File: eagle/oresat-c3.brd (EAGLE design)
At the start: 99.8 x 94.6 mm, 411 parts, among them IC2 STM32F439VIT6_PORT_BREAKOUT, J5 ORESAT-DEBUG-CONNECTOR-ALL, J6 J-SAMTEC-TFM-120-X1-XXX-D-RA, Q1 MOSFET-PCH-SOT23-6, Q10 PMOS, Q11 FDMQ86530L_2-GATES, Q12 MOSFET-PCH-SOT23-6, Q13 MOSFET-PCH-SOT23-6, Q14 FDMQ86530L_2-GATES, Q2 NTR4101, Q4 P-CH, Q5 N-CH, Q6 MOSFET-PCH-SOT23-6, Q7 BFPXXXF, Q8 MOSFET-PCH-SOT23-6, Q9 BFPXXXF, U1 MAX892LEUA+T21-0036K-L, U10 SI4112, U11 U-ONSEMI-AX5043, U12 LP2985AIM5-1.8_NOPB, U13 U-ONSEMI-AX5043, U14 LP2985AIM5-1.8_NOPB, U15 Qorvo 856930, U16 MAC-24+, U17 BP0805A1308, U18 B8666, U19 BP0805A1308, U2 TCAN330, U20 BGB7XXL7ESD, U21 BP0805A1308, U22 TLV7041DCKRYC5, U23 LP2985AIM5-2.5_NOPB, U24 MAX941EUA+, U25 SN74LVC1G32QDBVRQ1, U26 TPS62112, U27 TPS259620, U28 LP2985AIM5-3.3_NOPB, U29 SN74LVC1G11IDCKRQ1, U3 TCAN330, U30 U-TQP7M9105, U31 BDCN-20-13+, U32 LT5534, U33 LT5534, U34 RV-3028-C7, U4 TPS259621, U5 TPS62111RSA, U6 LP2985AIM5-2.5_NOPB, U7 TLV1704AMPWPSEP, U8 QPC1022, U9 SFEM016GB1EM1TO-A-HG-111-STD, X1 ECS-160-10-36Q-ES-TR_16MHZ, X2 ABS07-32.768KHZ-T-SMD-2, X3 TAITIEN-TY, X4 TAITIEN-TY

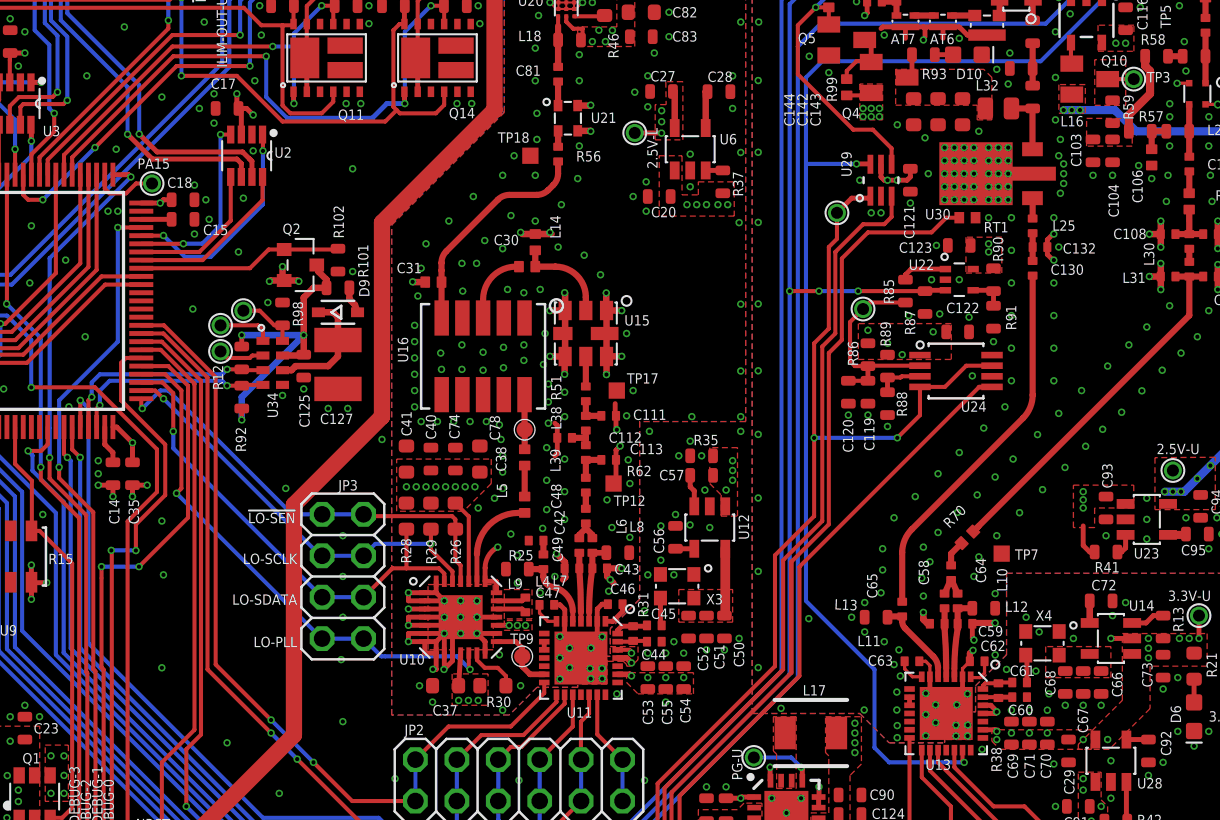
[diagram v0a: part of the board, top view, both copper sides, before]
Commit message: Added FRAM, because FRAMgit add oresat-c3.brd oresat-c3.sch, added 5th order LPF for UHF TX. Waiting on final values of LPF and time out timer (TOT) from Glenn, then need to fix attributes and ship!
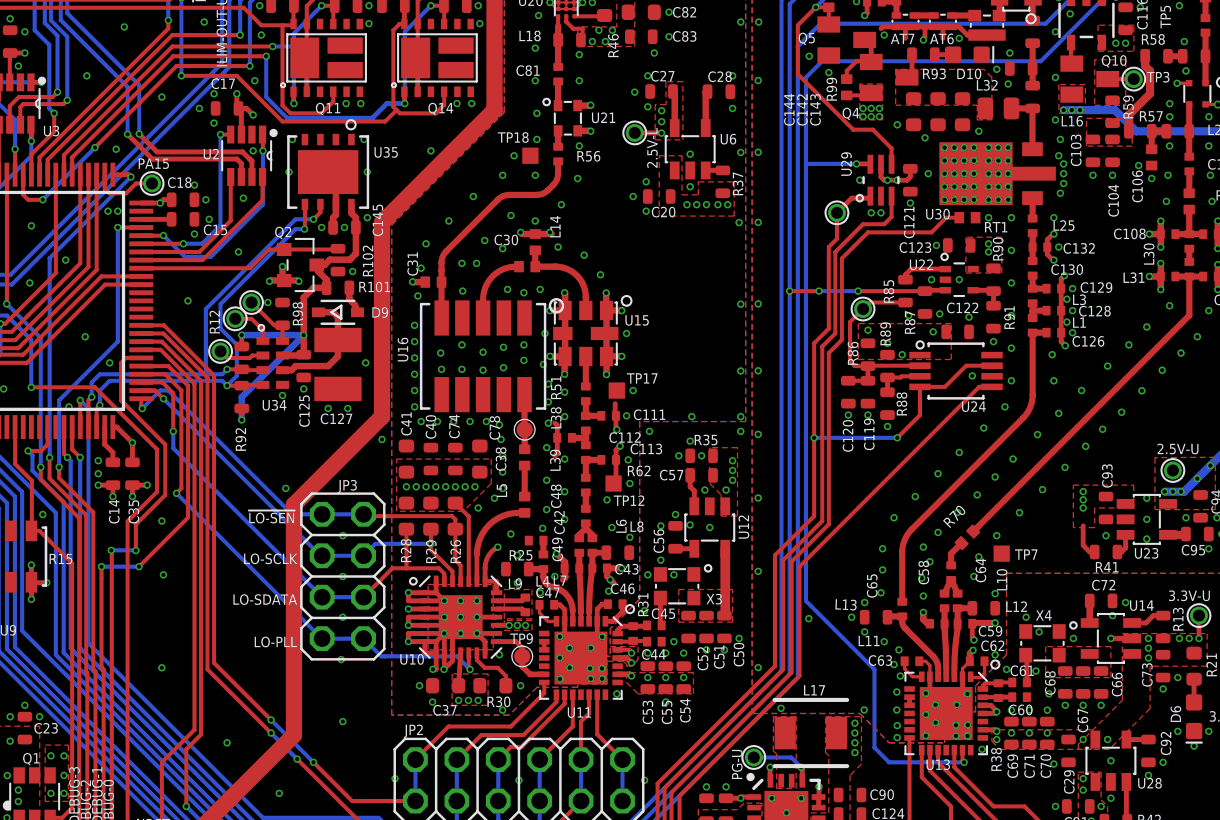
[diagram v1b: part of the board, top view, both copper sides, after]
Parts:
- added C126, C129: TBD1, oresat-rcl:.0402-C-NOSILK
- added C128: TBD3, oresat-rcl:.0402-C-NOSILK
- added C145: 0.1u, C3_SamacSys_Parts:.0603-C-NOSILK
- added L1, L3: TBD2, oresat-rcl:.0402-C-NOSILK
- added U35: FM24CL64B-DGTR, U-Cypress-FM24CLXXB-DGTR-I2C-FRAM-WFDM-8:TDFN-8
- U34: value RV-3028-C7 -> Micro Crystal RV-3028-C7
- moved TP24 0.98 mm to (33.6, 42.4)
- moved TP23 0.71 mm to (34.6, 43.4)
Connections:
- new net N$73: C128.1, L1.2, L3.1
- new net N$74: C129.1, C130.1, L3.2
- net GND: now also C145.2, U35.1, U35.2, U35.3, U35.4, U35.7, U35.9
- net GND-U: now also C126.2, C128.2, C129.2
- net RTC_I2C_SCL: now also U35.6
- net RTC_I2C_SDA: now also U35.5
- net RTC_PWR: now also C145.1, U35.8
- net TX-TO-PA: now also C126.1, L1.1; no longer C130.1
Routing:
- net RTC_I2C_SDA: track 12.7 -> 27.0 mm, vias 2 -> 3
- net RTC_I2C_SCL: track 13.7 -> 27.6 mm, vias 2 -> 3
- net RTC_PWR: track 20.1 -> 25.9 mm
- net GND-U: track 62.0 -> 66.4 mm, vias 325 -> 330
- net GND: track 63.9 -> 67.5 mm, vias 347 -> 356
- net TX-TO-PA: track 23.1 -> 20.4 mm
- net N$73: track 0.00 -> 1.75 mm
- net N$74: track 0.00 -> 1.65 mm
- net N$67: track 3.37 -> 2.64 mm

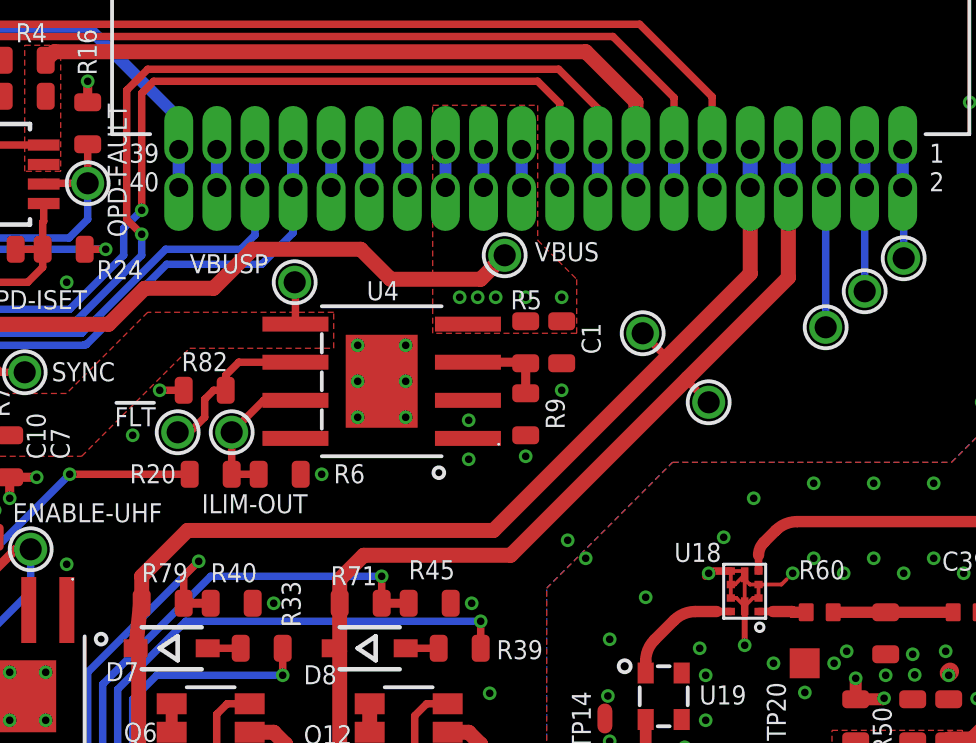
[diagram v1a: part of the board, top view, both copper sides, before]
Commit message: Added TVS protection on the deployer lines.
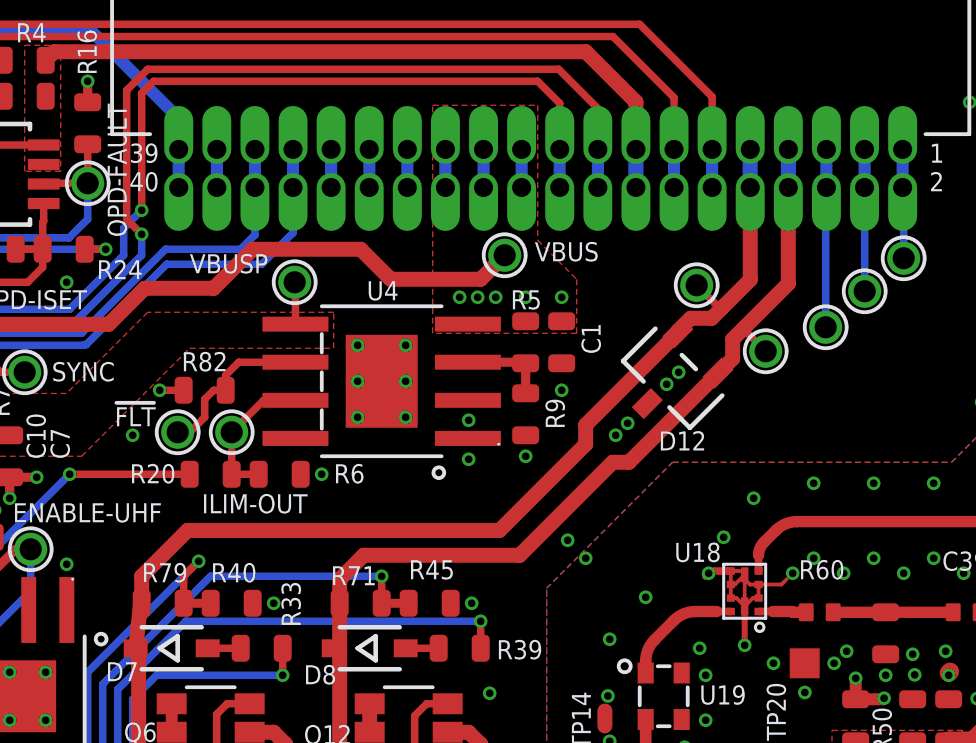
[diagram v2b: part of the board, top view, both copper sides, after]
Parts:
- added D12: MMBZ15VALFHT116, D-Rohm-MMBZ15VALFH-TVS-15V-two-channel:DIO_MMBZ1_ROM
- moved H-DPLY 2.55 mm to (57.4, 81.8)
- moved T-DPLY 2.41 mm to (55.1, 84.0)
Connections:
- net GND: now also D12.3
- net HELI_DEPLOY: now also D12.1
- net TURN_DEPLOY: now also D12.2
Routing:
- net TURN_DEPLOY: track 43.0 -> 43.6 mm
- net GND: vias 356 -> 360

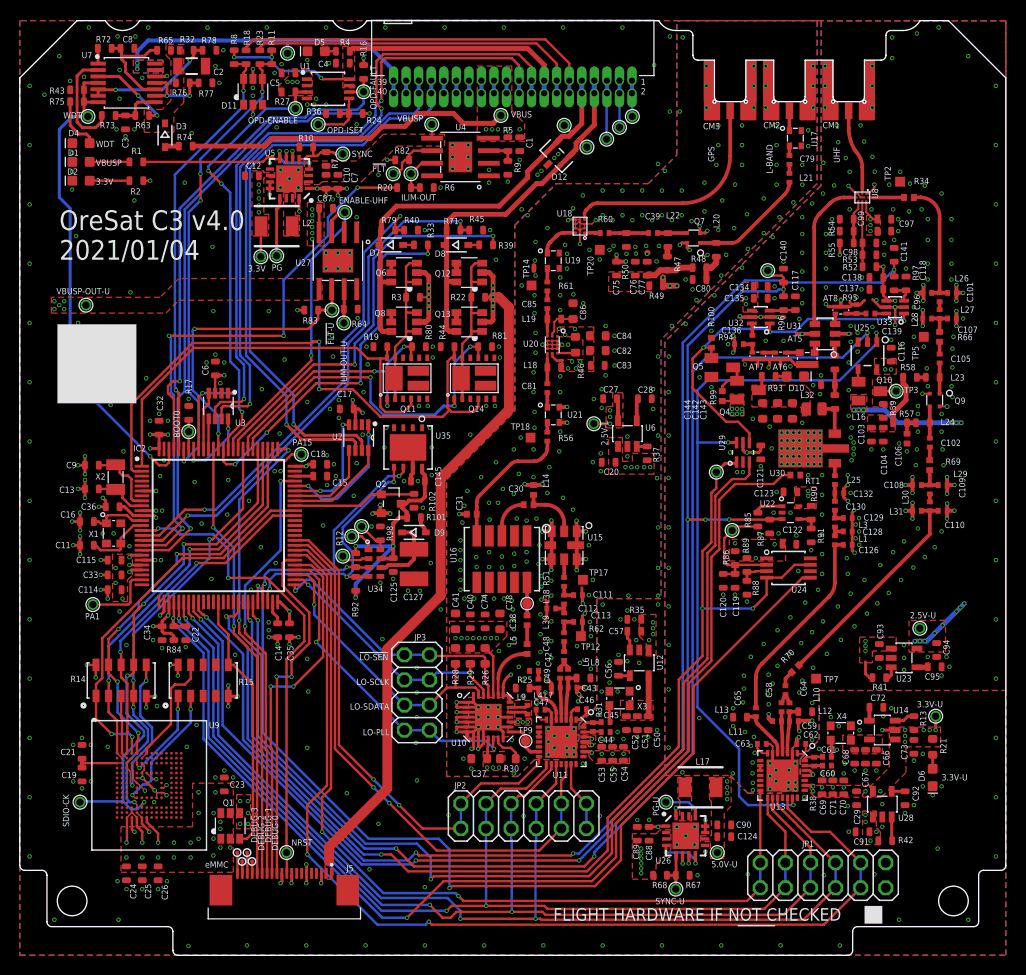
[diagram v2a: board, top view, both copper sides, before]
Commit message: Fixed up PA TSTOP and TCREAM, fixed quad nchannel TCREAM, added call signs of main C3 folks, fixed 2mm miter on RF lines.
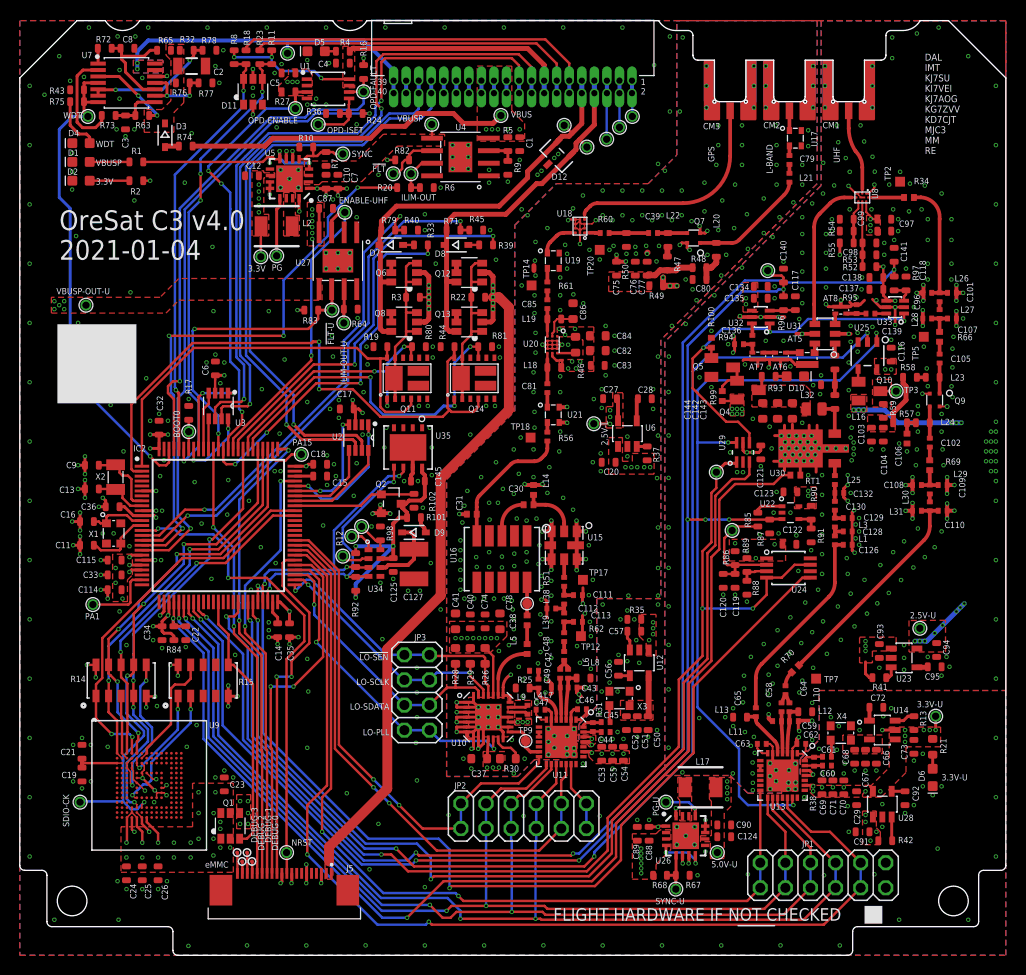
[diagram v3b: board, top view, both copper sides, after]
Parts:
- C126, C129: value TBD1 -> 18p
- C128: value TBD3 -> 12p
- L1, L3: value TBD2 -> 15n
- Q11, Q14: value FDMQ86530L_2-GATES -> FDMQ86530L
- Q12, Q13, Q6, Q8: value MOSFET-PCH-SOT23-6 -> DMP2240UDM-7
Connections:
- net RTC_I2C_SCL renamed I2CSYS_SCL
- net RTC_I2C_SDA renamed I2CSYS_SDA
- net RTC_PWROFF renamed I2CSYS_PWROFF
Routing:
- net GND-U: track 66.4 -> 73.6 mm, vias 330 -> 338
- net GND: vias 360 -> 362
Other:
- board text added: "2021-01-04"
- board text added: "DAL IMT KJ7SU KI7VEI KJ7AOG KG7ZVV KD7CJT MJC3 MM RE"
- board text removed: "2021/01/04"

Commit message: Updated date BOM for C3 V4, fixed some parts for future V5.
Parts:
- added R103: 100k, C3_SamacSys_Parts:.0603-C-NOSILK
- C144: device oresat-rcl:.0603-B-NOSILK -> oresat-rcl:.0603-C-NOSILK
- Q4: value P-CH -> NTR4101; device transistor-small-signal:SOT23 -> Q-MOSFET-PCH-SOT23-3:SOT23-3
- Q5: value N-CH -> PM45EN; device transistor-small-signal:SOT23 -> Q-MOSFET-NCH-SOT23-3:SOT23-3
- R101: value 100 -> 150
- R21: device oresat-rcl:.0603-B-NOSILK -> C3_SamacSys_Parts:.0603-C-NOSILK
- R52, R53, R54, R55, R93, R96, R97: device oresat-rcl:.0603-C-NOSILK -> C3_SamacSys_Parts:.0603-C-NOSILK
- R82: value NP/10K -> 10K
- R94, R95: value 47 -> 50
- U20: value BGB7XXL7ESD -> BGB741L7ESD
- moved Q5 0.10 mm to (71.0, 59.5)
- renumbered IC2 to U36
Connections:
- net !SD: now also R103.1
- net VBUS: now also R103.2
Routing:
- net !SD: track 33.1 -> 35.0 mm

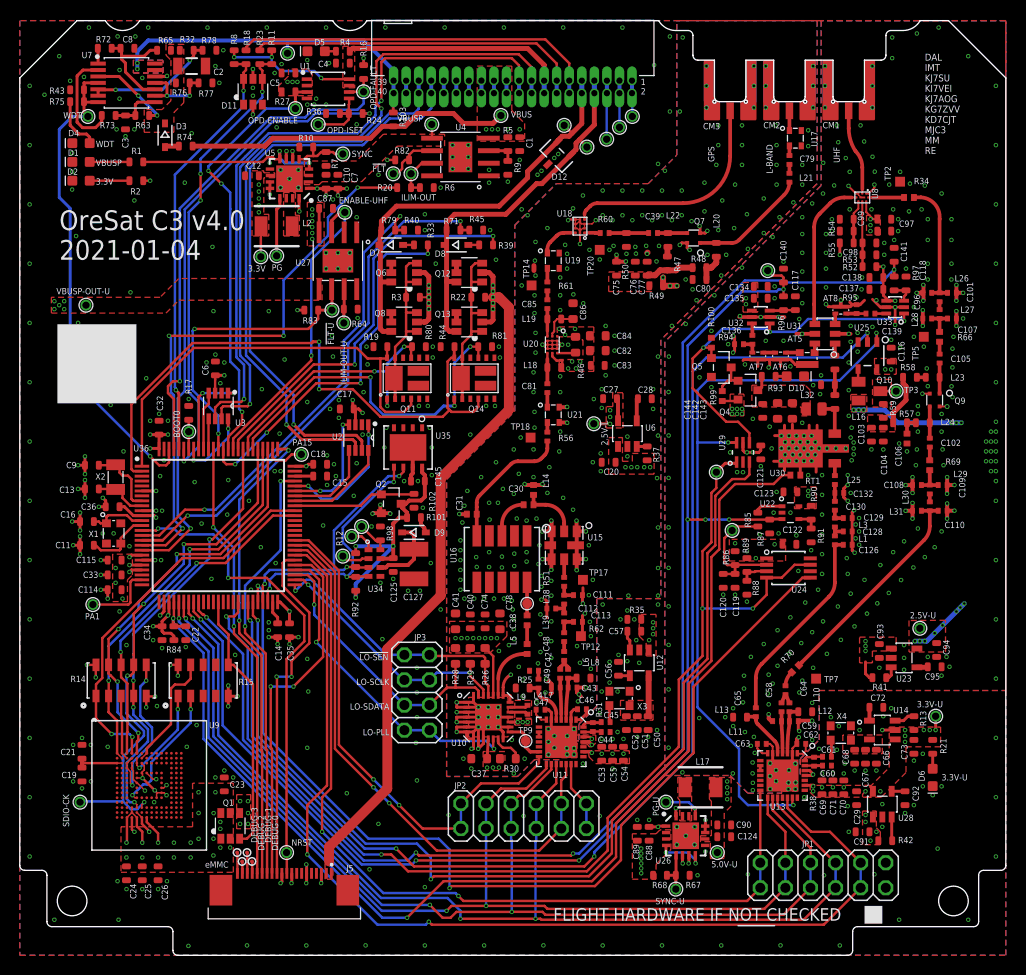
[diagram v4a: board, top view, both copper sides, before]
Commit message: Rev'd to version 5; added fiducials.
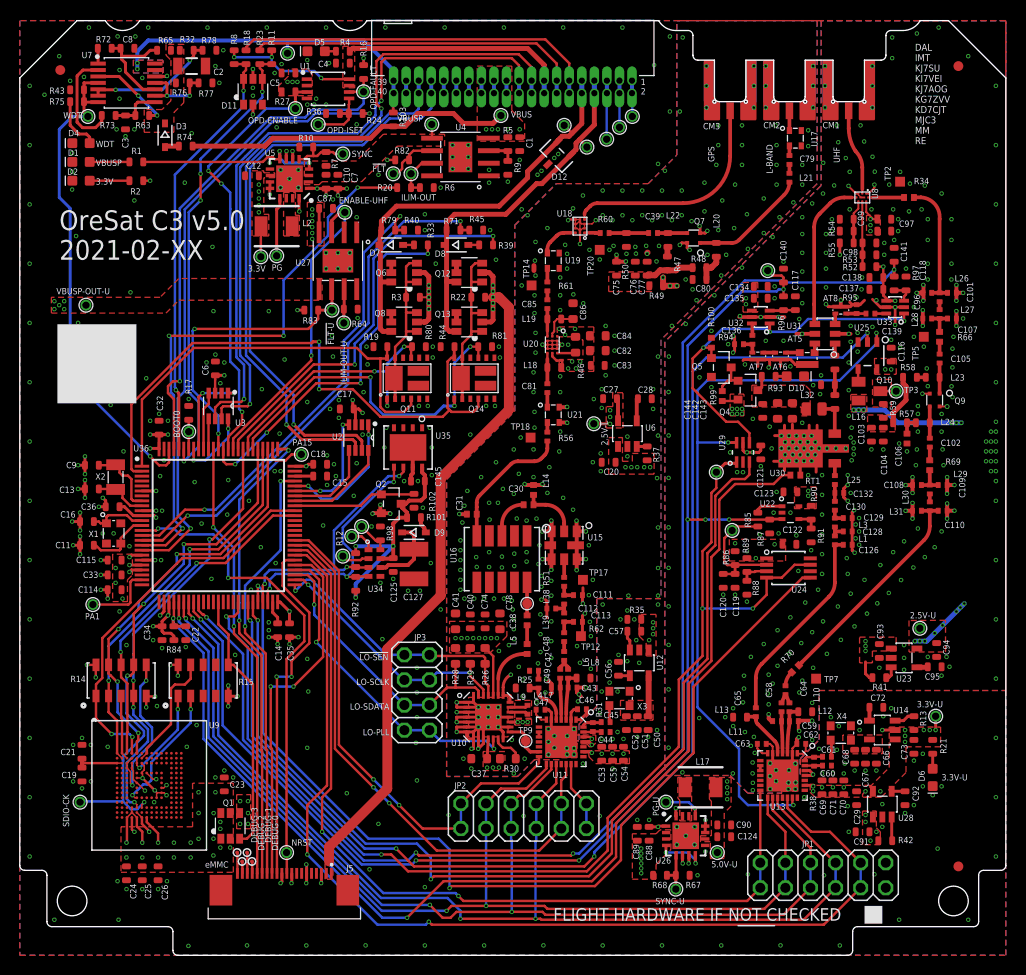
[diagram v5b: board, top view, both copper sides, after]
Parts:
- added FIDUCIAL1, FIDUCIAL2, FIDUCIAL3: FIDUCIAL-1.0X2.0, dock_v2:FIDUCIAL-1.0X2.0
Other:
- board text added: "2021-02-XX"
- board text added: "OreSat C3 v5.0"
- board text removed: "2021-01-04"
- board text removed: "OreSat C3 v4.0"

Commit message: Changes to the timeout timer based on available parts; updated SCH and BOM. Also fixed off-by-one-row errors for Mouser parts.
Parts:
- C119, C120: value 47u -> 22u
- R86: value 5.6k -> 10k

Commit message: Updated some names to be more explicit about logic levels.
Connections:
- net LBAND-LO-PLL renamed LBAND-PLL-!LOCKED
